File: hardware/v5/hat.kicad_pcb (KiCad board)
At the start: 2 copper layers, 65 x 56.5 mm, 24 parts, among them J1 GPIO, J2 Qwiic, J3 DB25 header, J4 V select, U1 CAT24C256, U2 SN74LVC161284DLR

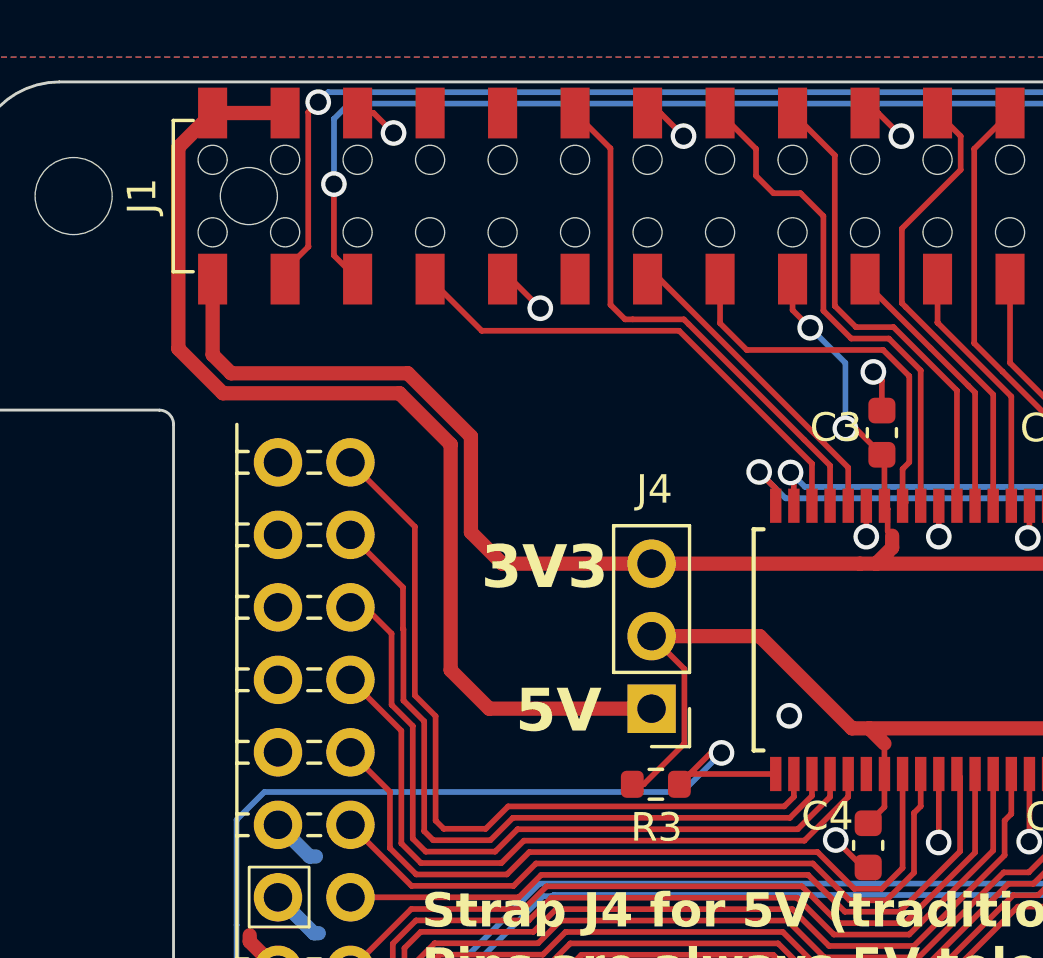
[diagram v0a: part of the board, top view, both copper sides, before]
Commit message: v5: switch J4 to SMT
Problem: the J4 1x3 header is a through hole part that is marked
"do not place" so it can be installed by hand.

Switch J4 to an SMT footprint and uncheck DNP.
Adjust board routing.
Add a LCSC part number to the BOM.
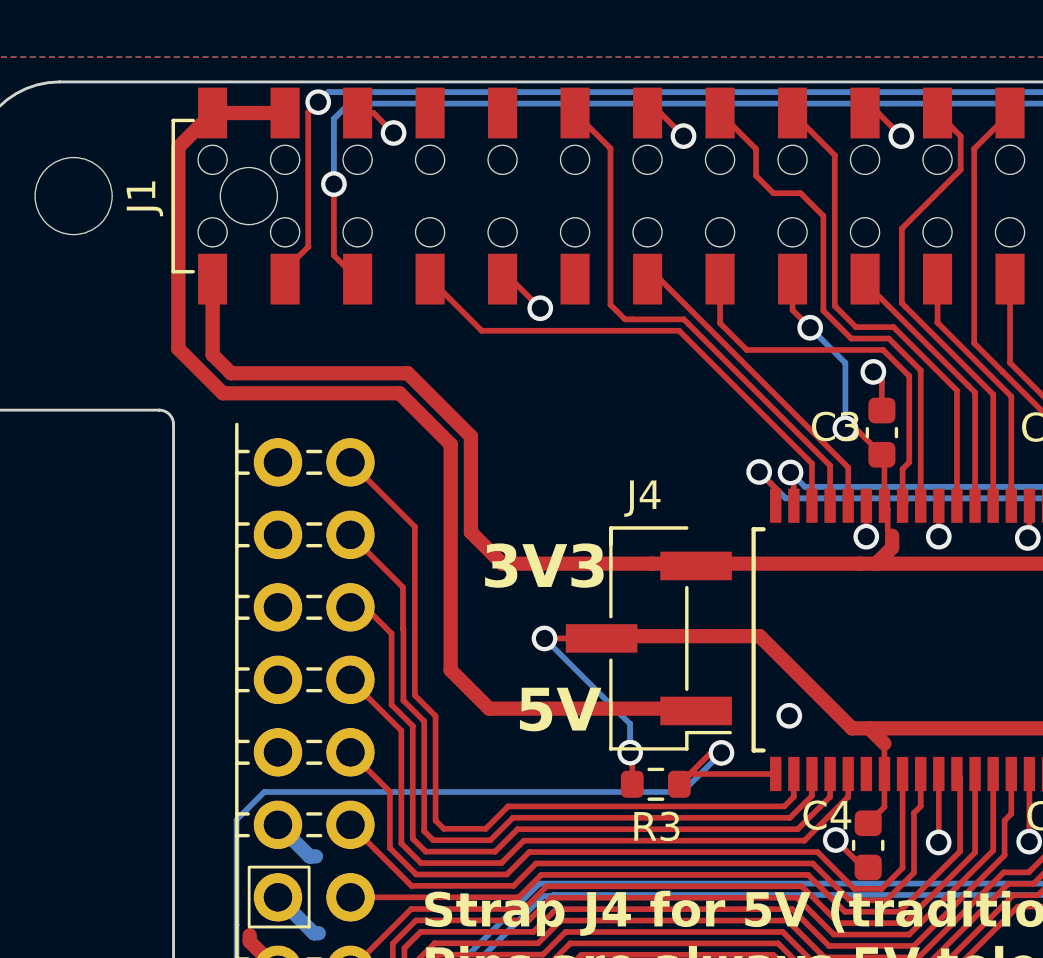
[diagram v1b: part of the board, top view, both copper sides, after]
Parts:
- J4: footprint Connector_PinHeader_2.54mm:PinHeader_1x03_P2.54mm_Vertical -> Connector_PinHeader_2.54mm:PinHeader_1x03_P2.54mm_Vertical_SMD_Pin1Left
- moved J4 2.46 mm to (123.7, 63.0)
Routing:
- net Net-(J4-Pin_2): track 29.9 -> 33.4 mm, vias 0 -> 2
- net +5V: track 37.7 -> 39.3 mm

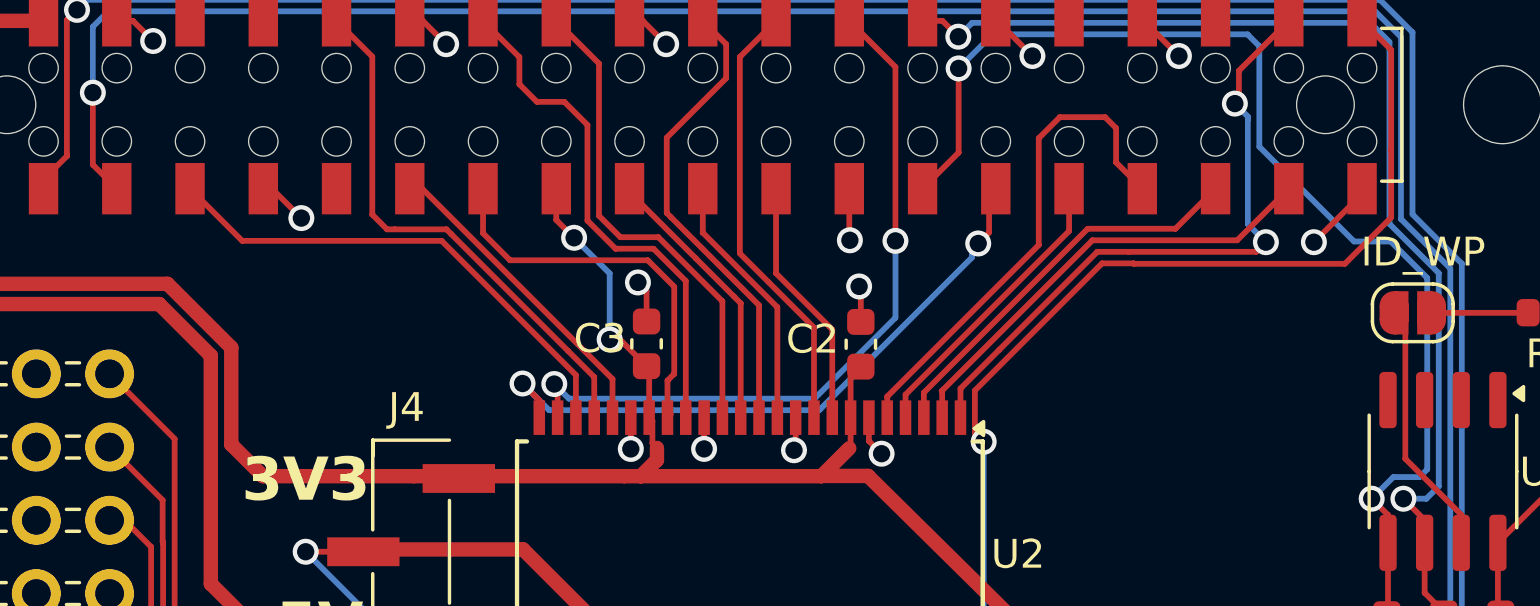
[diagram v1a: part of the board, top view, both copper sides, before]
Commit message: v5: put URL on the front of the board
Problem: URL for design files/software is not visible when
the board is installed.

Move to front of board.
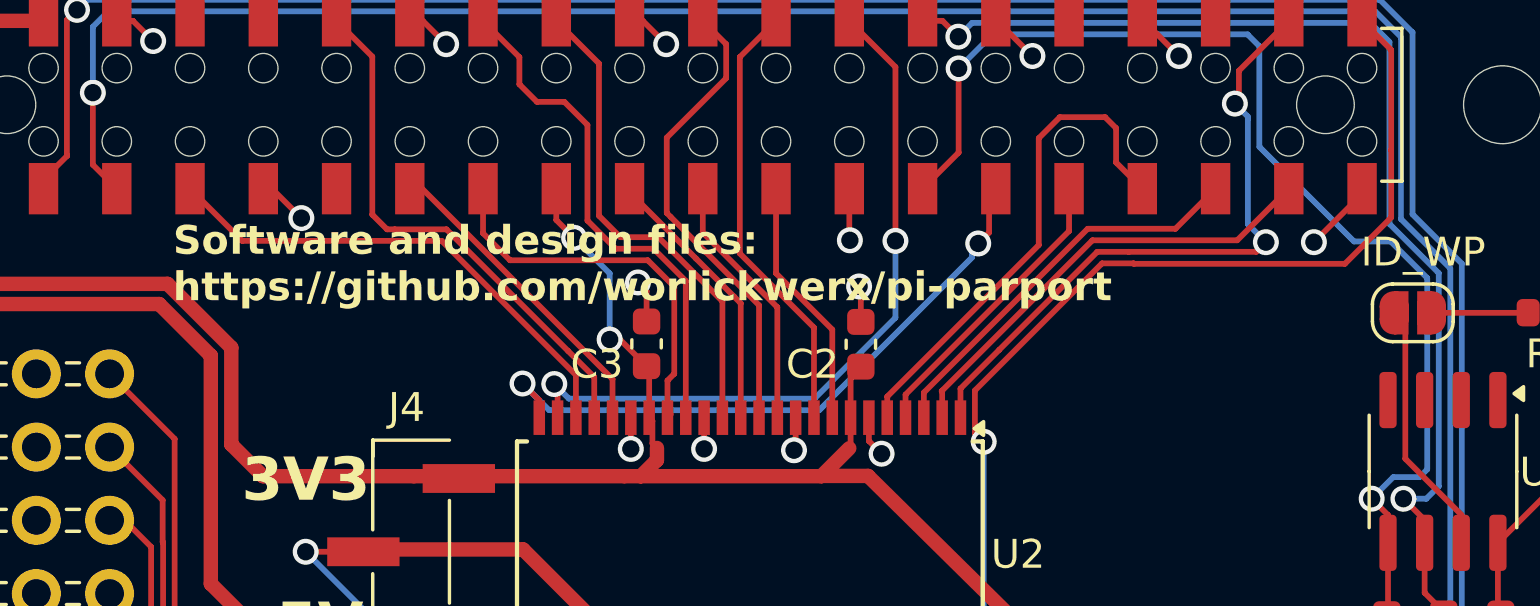
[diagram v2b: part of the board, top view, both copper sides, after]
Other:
- board text added: "Software and design files: https://github.com/worlickwerx/pi-parport"
- board text removed: "Software and design files: https://github.com/worlickwerx/pi-parport/"
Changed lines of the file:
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@@
 		(tags "capacitor")
 		(property "Reference" "C2"
-			(at 0.175 -1.68 180)
+			(at -0.695 -1.68 180)
 			(layer "F.SilkS")
 			(effects
@@
 		(tags "capacitor")
 		(property "Reference" "C3"
-			(at 0.18 -1.61 0)
+			(at -0.71 -1.72 0)
 			(layer "F.SilkS")
 			(effects
@@
 		(layer "Edge.Cuts")
 	)
-	(gr_text "Software and design files:\nhttps://github.com/worlickwerx/pi-parport/"
-		(at 143.7 99.58 0)
-		(layer "B.SilkS")
-		(effects
-			(font
-				(size 1.2 1.2)
-				(thickness 0.2)
-				(bold yes)
-			)
-			(justify left bottom mirror)
-		)
-	)
 	(gr_text "(C)2024 WorlickWerx, LLC"
-		(at 143.94 95.36 0)
+		(at 136.8 99.4 0)
 		(layer "B.SilkS")
 		(effects
@@
 				(bold yes)
 			)
+			(justify left bottom)
+		)
+	)
+	(gr_text "Software and design files:\nhttps://github.com/worlickwerx/pi-parport"
+		(at 115.4 54.4 0)
+		(layer "F.SilkS")
+		(effects
+			(font
+				(size 1 1)
+				(thickness 0.17)
+				(bold yes)
+			)

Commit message: v5: add hardware license to silkscreen
Problem: on the back of the baord we have a copyright notice
but not a license designator.

Add the license.
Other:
- board text added: "CERN-OHL-1.2"
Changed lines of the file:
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@@
 		(layer "Edge.Cuts")
+	)
+	(gr_text "CERN-OHL-1.2"
+		(at 136.7 97.3 0)
+		(layer "B.SilkS")
+		(effects
+			(font
+				(size 1.2 1.2)
+				(thickness 0.2)
+				(bold yes)
+			)
+			(justify left bottom mirror)
+		)
 	)
 	(gr_text "(C)2024 WorlickWerx, LLC"

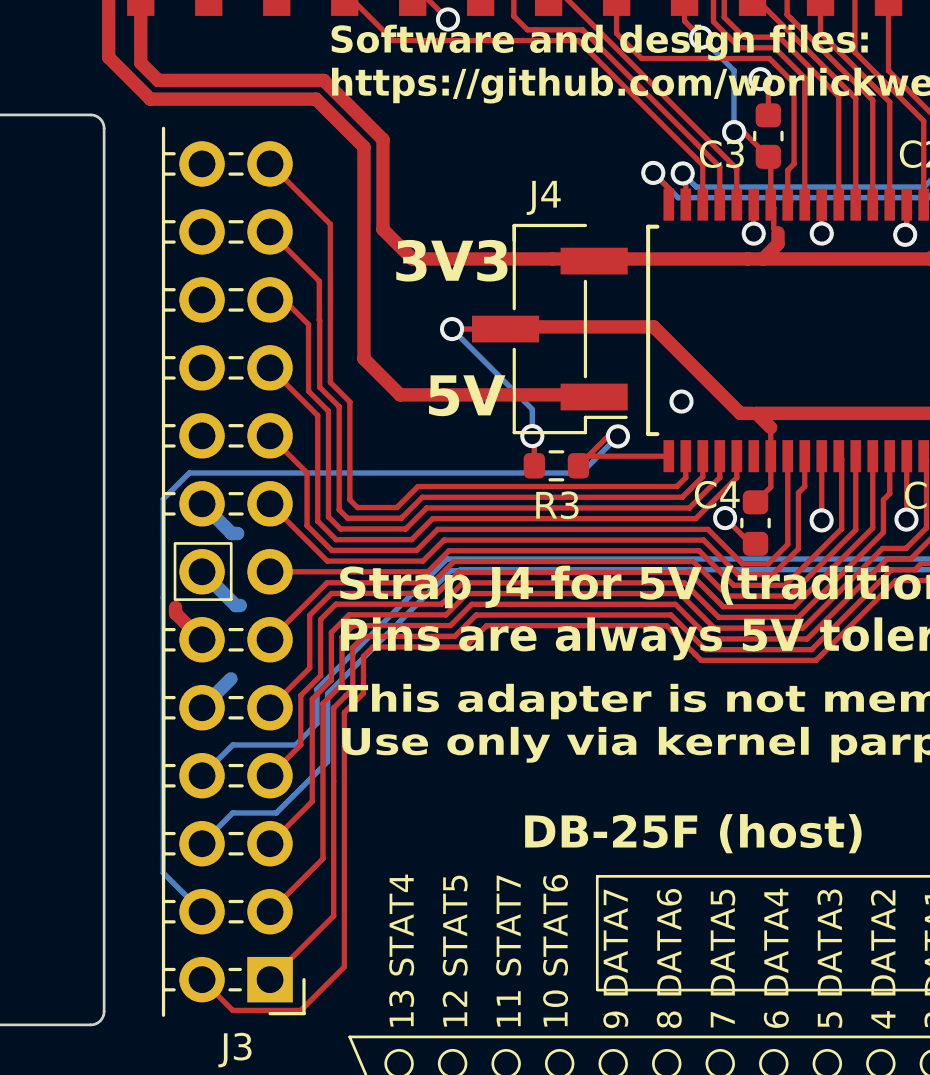
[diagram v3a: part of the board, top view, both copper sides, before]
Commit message: v5: adjust board layout for easy rework
Problem: J4 is too close to U2 to permit easy rework.

Move it away from U2 a bit and reroute.
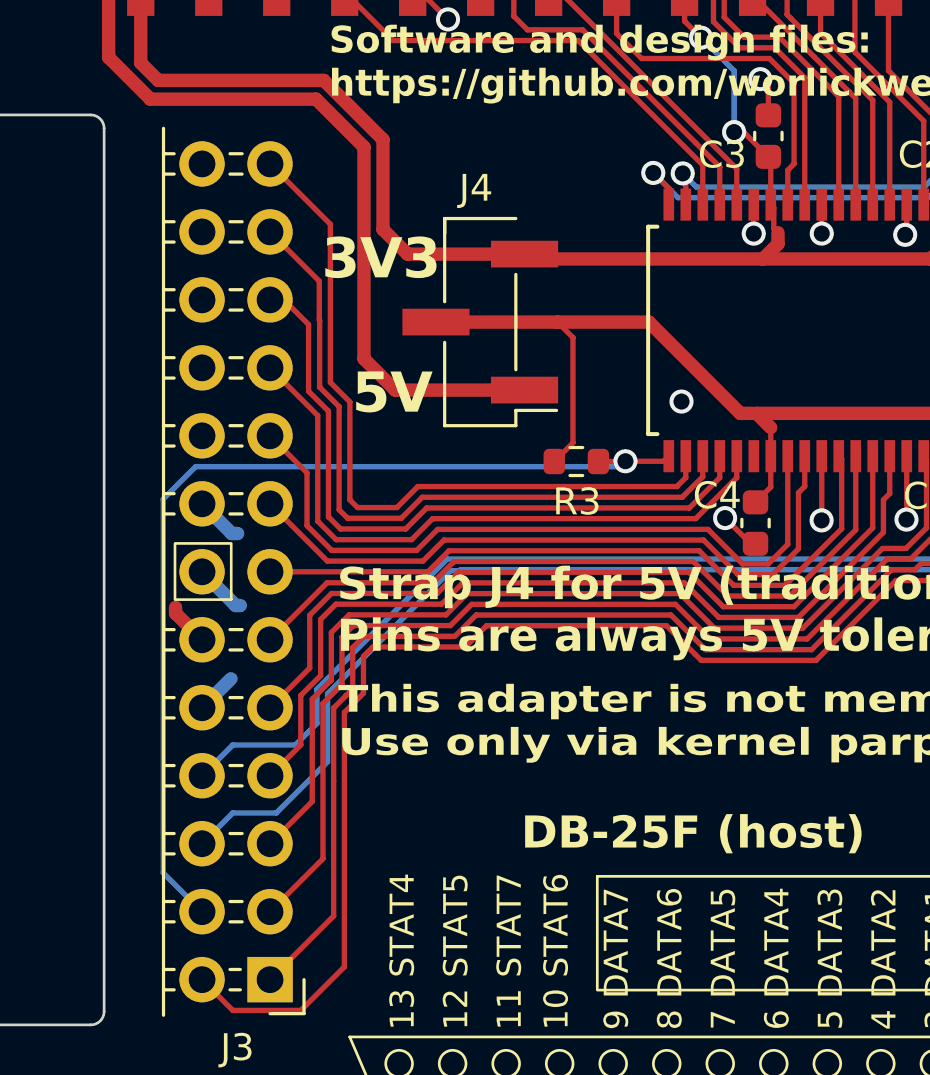
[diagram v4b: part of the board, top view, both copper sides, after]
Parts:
- moved J4 2.61 mm to (121.1, 62.7)
- moved R3 0.76 mm to (124.6, 68.0)
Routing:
- net /STATUS3: track 39.4 -> 36.6 mm
- net +5V: track 39.3 -> 36.6 mm
- net Net-(J4-Pin_2): vias 2 -> 0
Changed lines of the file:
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@@
 	(footprint "Connector_PinHeader_2.54mm:PinHeader_1x03_P2.54mm_Vertical_SMD_Pin1Left"
 		(layer "F.Cu")
-		(at 123.655 63 180)
+		(at 121.055 62.74 180)
 		(descr "surface-mounted straight pin header, 1x03, 2.54mm pitch, single row, style 1 (pin 1 left)")
 		(tags "Surface mounted pin header SMD 1x03 2.54mm single row style1 pin1 left")
@@
 	(footprint "Resistor_SMD:R_0603_1608Metric"
 		(layer "F.Cu")
-		(at 123.9 68.11)
+		(at 124.645 67.95)
 		(descr "Resistor SMD 0603 (1608 Metric), square (rectangular) end terminal, IPC_7351 nominal, (Body size source: IPC-SM-782 page 72, https://www.pcb-3d.com/wordpress/wp-content/uploads/ipc-sm-782a_amendment_1_and_2.pdf), generated with kicad-footprint-generator")
 		(tags "resistor")
@@
 	)
 	(gr_text "5V"
-		(at 118.98 66.41 0)
+		(at 116.26 66.27 0)
 		(layer "F.SilkS")
 		(effects
@@
 	)
 	(gr_text "3V3"
-		(at 117.78 61.38 0)
+		(at 115.13 61.25 0)
 		(layer "F.SilkS")
 		(effects
@@
 	)
 	(segment
-		(start 117.42 59.28)
-		(end 118.52 60.38)
-		(width 0.5)
-		(layer "F.Cu")
-		(net 25)
-	)
-	(segment
 		(start 161.765 74.02)
 		(end 161.735 74.05)
@@
 	)
 	(segment
+		(start 122.89 60.38)
+		(end 122.71 60.2)
+		(width 0.5)
+		(layer "F.Cu")
+		(net 25)
+	)
+	(segment
 		(start 131.91 58.35)
 		(end 131.91 56.655)
@@
 	)
 	(segment
-		(start 123.75 60.38)
-		(end 131.05 60.38)
-		(width 0.5)
+		(start 161.44 65.14)
+		(end 164.17 67.87)
+		(width 0.2)
 		(layer "F.Cu")
 		(net 25)
 	)
 	(segment
-		(start 161.44 65.14)
-		(end 164.17 67.87)
-		(width 0.2)
+		(start 117.42 59.28)
+		(end 118.34 60.2)
+		(width 0.5)
 		(layer "F.Cu")
 		(net 25)
@@
 	)
 	(segment
-		(start 131.05 60.38)
-		(end 131.62 60.38)
-		(width 0.5)
-		(layer "F.Cu")
-		(net 25)
-	)
-	(segment
 		(start 138.895 56.935)
 		(end 139.25 56.58)
@@
 	)
 	(segment
-		(start 118.52 60.38)
-		(end 123.75 60.38)
-		(width 0.5)
-		(layer "F.Cu")
-		(net 25)
-	)
-	(segment
 		(start 164.04 59.99)
 		(end 161.34 62.69)
@@
 	)
 	(segment
+		(start 131.62 60.38)
+		(end 122.89 60.38)
+		(width 0.5)
+		(layer "F.Cu")
+		(net 25)
+	)
+	(segment
 		(start 131.91 56.655)
 		(end 131.82 56.565)
@@
 	)
 	(segment
+		(start 118.34 60.2)
+		(end 122.71 60.2)
+		(width 0.5)
+		(layer "F.Cu")
+		(net 25)
+	)
+	(segment
 		(start 138.895 59.365)
 		(end 138.85 59.41)
@@
 	)
 	(segment
-		(start 116.71 64.11)
-		(end 118.06 65.46)
-		(width 0.5)
-		(layer "F.Cu")
-		(net 29)
-	)
-	(segment
 		(start 108.37 44.59)
 		(end 107.17 45.79)
@@
 	)
 	(segment
-		(start 108.73005 54.41)
-		(end 114.92 54.41)
+		(start 117.88 65.28)
+		(end 122.71 65.28)
 		(width 0.5)
 		(layer "F.Cu")
@@
 	)
 	(segment
-		(start 125.23 65.46)
-		(end 125.31 65.54)
+		(start 108.73005 54.41)
+		(end 114.92 54.41)
 		(width 0.5)
 		(layer "F.Cu")
@@
 	)
 	(segment
-		(start 118.06 65.46)
-		(end 125.23 65.46)
+		(start 116.71 64.11)
+		(end 117.88 65.28)
 		(width 0.5)
 		(layer "F.Cu")
@@
 	)
 	(segment
-		(start 126.2 67.01)
-		(end 125.825 67.01)
+		(start 125.47 67.95)
+		(end 126.47 67.95)
 		(width 0.2)
 		(layer "F.Cu")
@@
 	)
 	(segment
-		(start 125.085 67.75)
-		(end 124.725 68.11)
+		(start 127.91 67.94)
+		(end 128.1 67.75)
 		(width 0.2)
 		(layer "F.Cu")
@@
 	)
 	(segment
-		(start 125.825 67.01)
-		(end 124.725 68.11)
+		(start 126.48 67.94)
+		(end 127.91 67.94)
 		(width 0.2)
 		(layer "F.Cu")
@@
 	)
 	(segment
-		(start 128.1 67.75)
-		(end 125.085 67.75)
+		(start 126.47 67.95)
+		(end 126.48 67.94)
 		(width 0.2)
 		(layer "F.Cu")
@@
 	)
 	(via
-		(at 126.2 67.01)
+		(at 126.48 67.94)
 		(size 0.9)
 		(drill 0.6)
@@
 	(segment
 		(start 109.21 69.353654)
-		(end 110.183654 68.38)
-		(width 0.2)
-		(layer "B.Cu")
-		(net 37)
-	)
-	(segment
-		(start 110.66 84.77)
 		(end 109.21 83.32)
 		(width 0.2)
@@
 	)
 	(segment
-		(start 110.183654 68.38)
-		(end 124.83 68.38)
+		(start 126.28 68.14)
+		(end 110.423654 68.14)
 		(width 0.2)
 		(layer "B.Cu")
@@
 	)
 	(segment
-		(start 109.21 73.04)
-		(end 109.21 69.353654)
+		(start 109.21 83.32)
+		(end 110.66 84.77)
 		(width 0.2)
 		(layer "B.Cu")
@@
 	)
 	(segment
-		(start 124.83 68.38)
-		(end 126.2 67.01)
+		(start 126.48 67.94)
+		(end 126.28 68.14)
 		(width 0.2)
 		(layer "B.Cu")
@@
 	)
 	(segment
-		(start 109.21 83.32)
-		(end 109.21 73.04)
+		(start 110.423654 68.14)
+		(end 109.21 69.353654)
 		(width 0.2)
 		(layer "B.Cu")
@@
 	)
 	(segment
-		(start 131.23 66.15)
-		(end 130.77 66.15)
-		(width 0.5)
+		(start 124.52 67.25)
+		(end 124.52 63.32)
+		(width 0.2)
 		(layer "F.Cu")
 		(net 53)
@@
 	)
 	(segment
+		(start 130.77 66.15)
+		(end 127.36 62.74)
+		(width 0.5)
+		(layer "F.Cu")
+		(net 53)
+	)
+	(segment
 		(start 131.375 66.15)
 		(end 131.91 66.685)
@@
 	)
 	(segment
+		(start 131.23 66.15)
+		(end 130.77 66.15)
+		(width 0.5)
+		(layer "F.Cu")
+		(net 53)
+	)
+	(segment
 		(start 139.24 69.46)
 		(end 138.895 69.115)
@@
 	)
 	(segment
-		(start 123.075 67.075)
-		(end 123 67)
-		(width 0.2)
-		(layer "F.Cu")
-		(net 53)
-	)
-	(segment
-		(start 123.075 68.11)
-		(end 123.075 67.075)
-		(width 0.2)
-		(layer "F.Cu")
-		(net 53)
-	)
-	(segment
-		(start 127.54 62.92)
-		(end 122.08 62.92)
-		(width 0.5)
-		(layer "F.Cu")
-		(net 53)
-	)
-	(segment
 		(start 131.34 69.475)
 		(end 131.91 68.905)
@@
 	)
 	(segment
-		(start 138.87 66.66)
-		(end 138.87 66.81)
+		(start 123.94 62.74)
+		(end 119.4 62.74)
 		(width 0.5)
 		(layer "F.Cu")
@@
 	)
 	(segment
-		(start 122.08 62.92)
-		(end 122 63)
+		(start 138.87 66.66)
+		(end 138.87 66.81)
 		(width 0.5)
 		(layer "F.Cu")
@@
 	)
 	(segment
-		(start 120 63)
-		(end 122 63)
+		(start 124.52 63.32)
+		(end 123.94 62.74)
 		(width 0.2)
 		(layer "F.Cu")
@@
 	)
 	(segment
-		(start 130.77 66.15)
-		(end 127.54 62.92)
+		(start 127.36 62.74)
+		(end 123.94 62.74)
 		(width 0.5)
 		(layer "F.Cu")
 		(net 53)
 	)
-	(via
-		(at 123 67)
-		(size 0.9)
-		(drill 0.6)
-		(layers "F.Cu" "B.Cu")
-		(net 53)
-	)
-	(via
-		(at 120 63)
-		(size 0.9)
-		(drill 0.6)
-		(layers "F.Cu" "B.Cu")
-		(net 53)
-	)
 	(segment
-		(start 123 66)
-		(end 120 63)
+		(start 123.82 67.95)
+		(end 124.52 67.25)
 		(width 0.2)
-		(layer "B.Cu")
-		(net 53)
-	)
-	(segment
-		(start 123 67)
-		(end 123 66)
-		(width 0.2)
-		(layer "B.Cu")
+		(layer "F.Cu")
 		(net 53)
 	)
